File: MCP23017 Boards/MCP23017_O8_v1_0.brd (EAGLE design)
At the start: 90 x 90 mm, 83 parts, among them IC3 74HC540N, IC4 74HC540N, IC5 MCP23017SP, X4 057-016-0

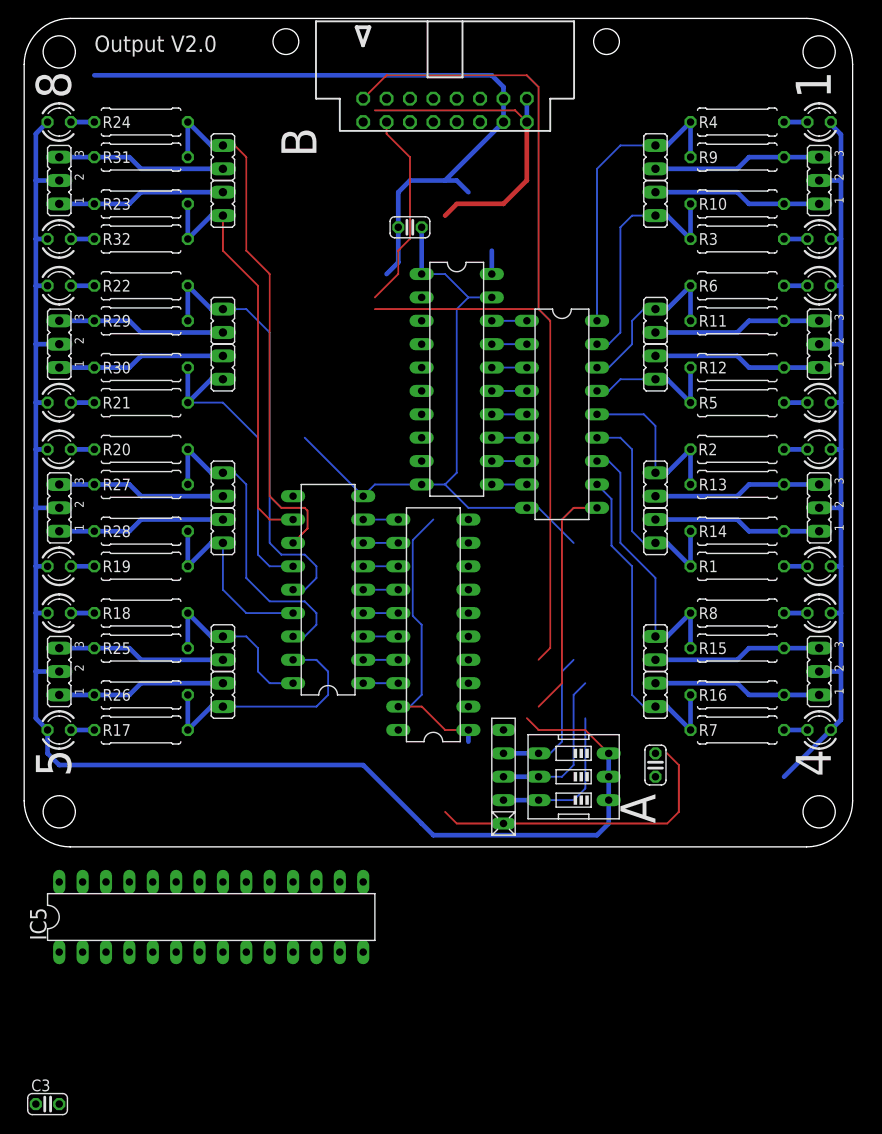
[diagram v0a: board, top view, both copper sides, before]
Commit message: Update MCP23017_O8_v1_0.brd
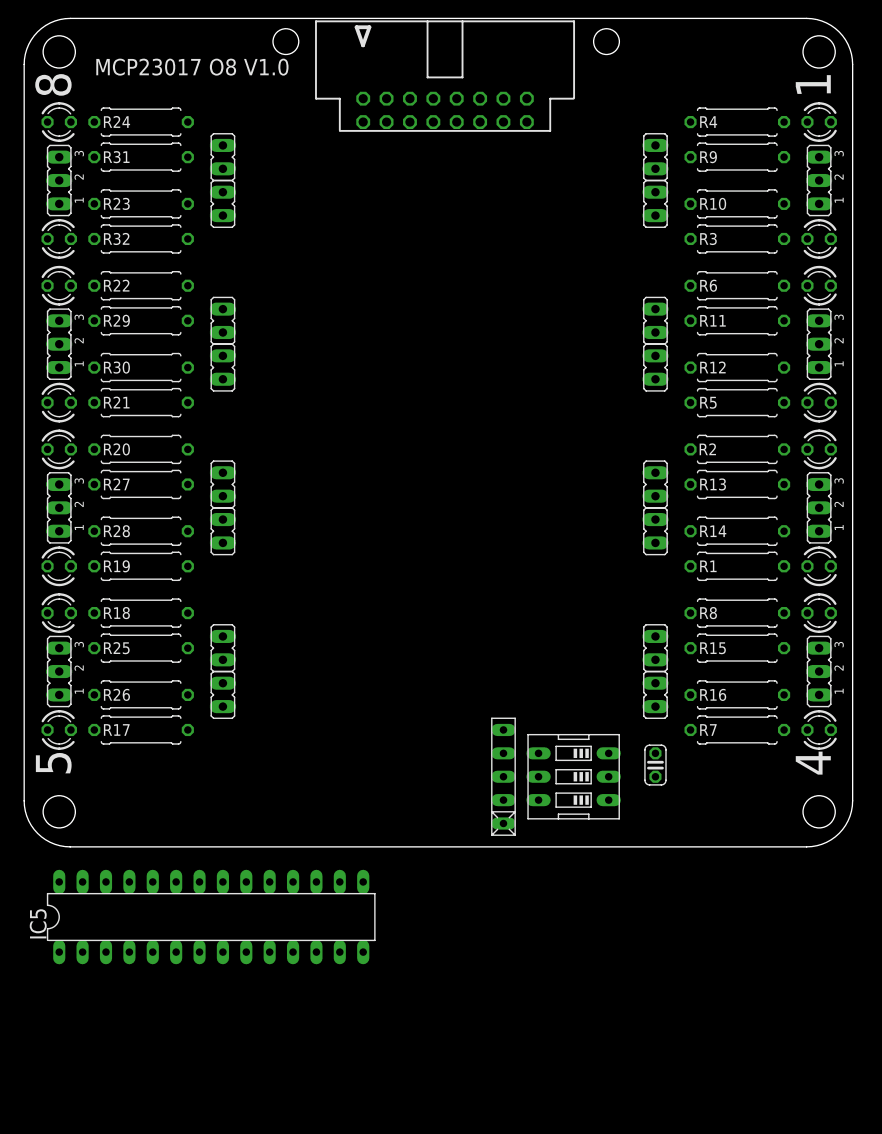
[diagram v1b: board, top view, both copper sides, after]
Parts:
- removed C3, C6: 100nF, resistor:C025-024X044
- removed IC1, IC2: (no value), uln-udn:DIL18
- removed IC3, IC4: 74HC540N, 74xx-eu:DIL20
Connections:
- removed net N$12: IC2.8, IC3.11
- removed net N$14: IC2.7, IC3.12
- removed net N$15: IC2.6, IC3.13
- removed net N$16: IC2.5, IC3.14
- removed net N$17: IC2.4, IC3.15
- removed net N$18: IC2.3, IC3.16
- removed net N$19: IC2.2, IC3.17
- removed net N$2: IC2.13, JP13.2, R1.2, R14.1
- removed net N$20: IC2.1, IC3.18
- removed net N$21: IC3.2, IC5.21
- removed net N$23: IC3.4, IC5.23
- removed net N$25: IC3.6, IC5.25
- removed net N$27: IC3.8, IC5.27
- removed net N$31: IC2.17, JP16.2, R10.1, R3.2
- removed net N$34: IC1.8, IC4.11
- removed net N$38: IC2.11, JP15.2, R16.1, R7.2
- removed net N$39: IC1.7, IC4.12
- removed net N$40: IC1.6, IC4.13
- removed net N$42: IC2.15, JP11.2, R12.1, R5.2
- removed net N$44: IC1.5, IC4.14
- removed net N$45: IC1.4, IC4.15
- removed net N$46: IC1.3, IC4.16
- removed net N$47: IC1.2, IC4.17
- removed net N$48: IC1.1, IC4.18
- removed net N$50: IC4.3, IC5.2
- removed net N$52: IC4.5, IC5.4
- removed net N$55: IC4.6, IC5.5
- removed net N$57: IC4.8, IC5.7
- removed net N$59: IC1.18, JP17.2, R18.2, R25.1
- removed net N$63: IC1.16, JP18.2, R20.2, R27.1
- removed net N$68: IC1.13, JP21.2, R21.2, R30.1
- removed net N$83: IC1.11, JP23.2, R23.2, R32.1
- net GND2: no longer C3.1, C6.1, IC1.9, IC2.9, IC3.1, IC3.10, IC3.19, IC4.1, IC4.10, IC4.19
- net N$22: now also JP16.2, R10.1, R3.2; no longer IC3.3
- net N$24: now also JP11.2, R12.1, R5.2; no longer IC3.5
- net N$26: now also JP13.2, R1.2, R14.1; no longer IC3.7
- net N$28: now also JP15.2, R16.1, R7.2; no longer IC3.9
- net N$29: now also IC5.21; no longer IC2.18
- net N$41: now also IC5.23; no longer IC2.16
- net N$43: now also IC5.25; no longer IC2.14
- net N$49: now also JP17.2, R18.2, R25.1; no longer IC4.2
- net N$5: now also IC5.27; no longer IC2.12
- net N$51: now also JP18.2, R20.2, R27.1; no longer IC4.4
- net N$56: now also JP21.2, R21.2, R30.1; no longer IC4.7
- net N$58: now also JP23.2, R23.2, R32.1; no longer IC4.9
- net N$60: now also IC5.2; no longer IC1.17
- net N$64: now also IC5.4; no longer IC1.15
- net N$65: now also IC5.5; no longer IC1.14
- net N$71: now also IC5.7; no longer IC1.12
- net VCC5.1: no longer C3.2, C6.2, IC1.10, IC2.10, IC3.20, IC4.20
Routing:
- net VCC5.1: track 365.0 -> 0.00 mm
- net GND2: track 173.2 -> 0.00 mm
- net N$82: track 101.7 -> 0.00 mm
- net N$71: track 58.5 -> 0.00 mm
- net N$65: track 48.1 -> 0.00 mm
- net N$83: track 46.3 -> 0.00 mm
- net N$38: track 36.2 -> 0.00 mm
- net N$63: track 35.4 -> 0.00 mm
- net N$68: track 34.9 -> 0.00 mm
- net N$29: track 32.6 -> 0.00 mm
- net N$5: track 31.1 -> 0.00 mm
- net N$60: track 27.5 -> 0.00 mm
- net N$31: track 27.5 -> 0.00 mm
- net N$2: track 25.0 -> 0.00 mm
- net N$64: track 22.4 -> 0.00 mm
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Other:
- board text added: "MCP23017 O8 V1.0"
- board text removed: "A"
- board text removed: "B"
- board text removed: "Output V2.0"

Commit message: Update MCP23017_O8_v1_0.brd
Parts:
- moved C2 63.2 mm to (44.5, 67.3), turned to 0 degrees
- moved IC5 58.5 mm to (44.5, 45.7), turned to 270 degrees
- moved RN2 15.3 mm to (50.8, 22.9), turned to 0 degrees
- moved SW1 10.2 mm to (50.8, 12.7), turned to 0 degrees

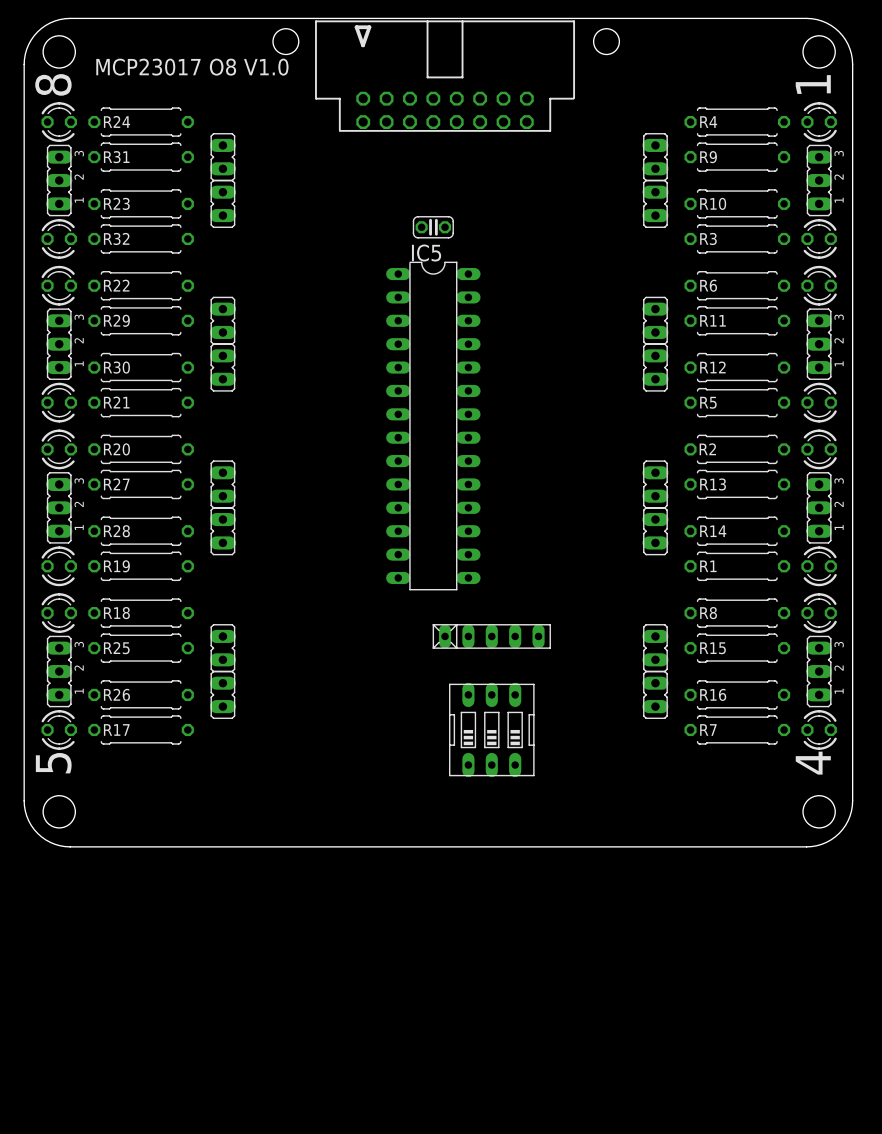
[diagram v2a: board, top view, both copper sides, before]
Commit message: Update MCP23017_O8_v1_0.brd
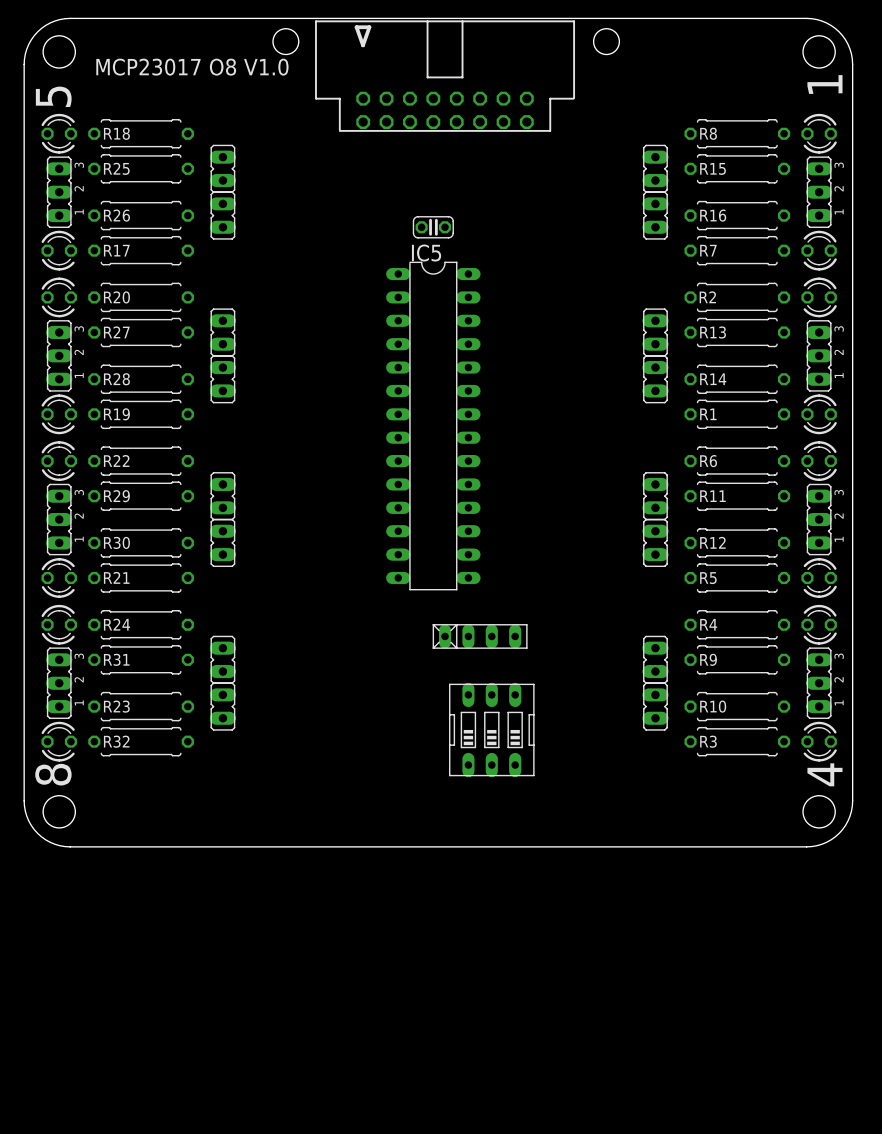
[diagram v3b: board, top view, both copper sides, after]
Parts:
- RN2: device resistor-net:RN-5 -> resistor-net_edit:RN-3
- moved JP22 54.6 mm to (21.6, 20.3)
- moved JP9 54.6 mm to (68.6, 20.3)
- moved R23 54.6 mm to (12.7, 11.4)
- moved R3 54.6 mm to (77.5, 11.4)
- moved R31 54.6 mm to (12.7, 20.3)
- moved R9 54.6 mm to (77.5, 20.3)
- moved SIG_15 54.6 mm to (3.81, 11.4)
- moved SIG_2 54.6 mm to (86.4, 11.4)
- moved JP1 54.6 mm to (86.4, 17.8)
- moved JP8 54.6 mm to (3.81, 17.8)
- moved R24 54.6 mm to (12.7, 24.1)
- moved R4 54.6 mm to (77.5, 24.1)
- moved SIG_1 54.6 mm to (86.4, 24.1)
- moved SIG_16 54.6 mm to (3.81, 24.1)
- moved JP16 54.6 mm to (68.6, 15.2)
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
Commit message: Update MCP23017_O8_v1_0.brd
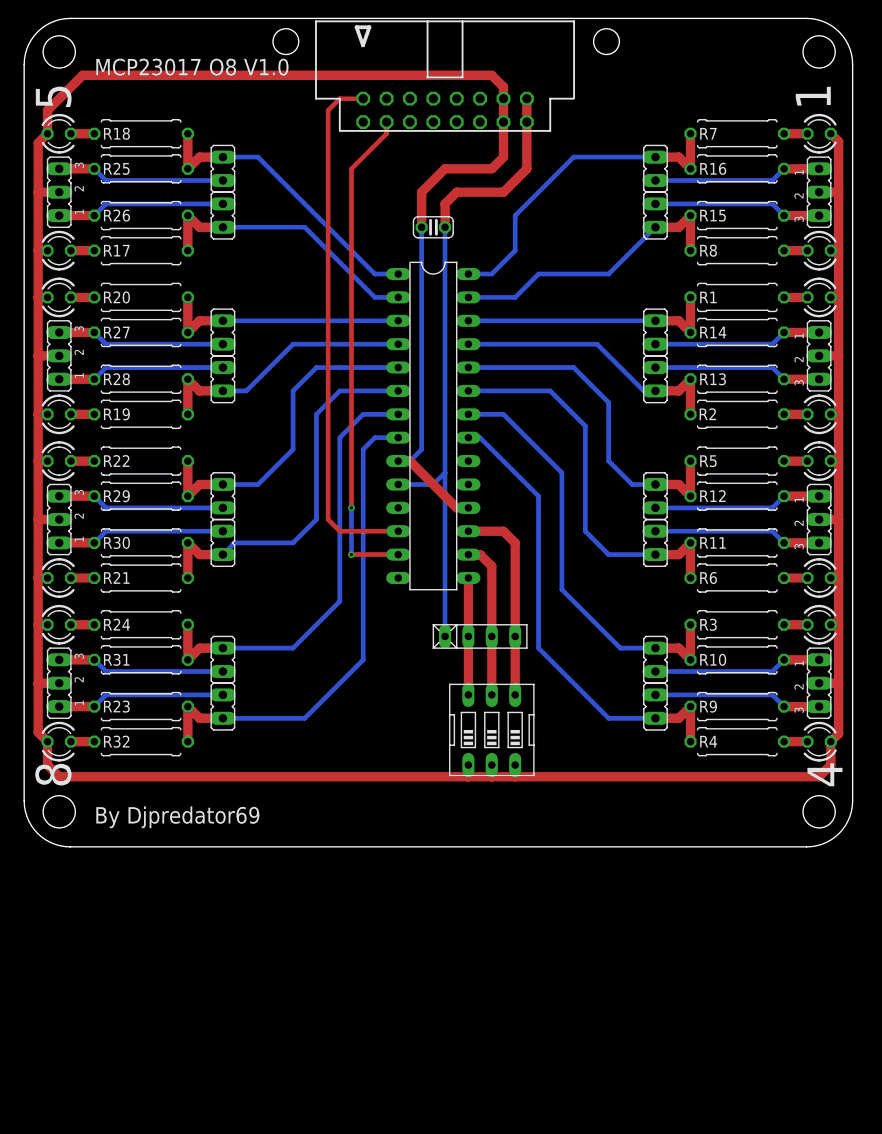
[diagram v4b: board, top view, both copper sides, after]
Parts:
- moved R7 12.7 mm to (77.5, 77.5)
- moved R8 12.7 mm to (77.5, 64.8)
- moved SIG_7 12.7 mm to (86.4, 64.8)
- moved SIG_8 12.7 mm to (86.4, 77.5)
- moved R3 12.7 mm to (77.5, 24.1)
- moved R4 12.7 mm to (77.5, 11.4)
- moved SIG_1 12.7 mm to (86.4, 11.4)
- moved SIG_2 12.7 mm to (86.4, 24.1)
- moved R1 12.7 mm to (77.5, 59.7)
- moved R2 12.7 mm to (77.5, 47.0)
- moved R5 12.7 mm to (77.5, 41.9)
- moved R6 12.7 mm to (77.5, 29.2)
- moved SIG_3 12.7 mm to (86.4, 29.2)
- moved SIG_4 12.7 mm to (86.4, 41.9)
- moved SIG_5 12.7 mm to (86.4, 47.0)
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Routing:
- net VCC5.1: track 0.00 -> 370.4 mm
- net GND2: track 0.00 -> 70.7 mm
- net N$82: track 0.00 -> 56.9 mm
- net N$84: track 0.00 -> 53.6 mm, vias 0 -> 2
- net N$58: track 0.00 -> 53.2 mm
- net N$29: track 0.00 -> 50.8 mm
- net N$71: track 0.00 -> 48.1 mm
- net N$22: track 0.00 -> 46.4 mm
- net N$41: track 0.00 -> 42.5 mm
- net N$56: track 0.00 -> 41.3 mm
- net N$24: track 0.00 -> 37.4 mm
- net N$65: track 0.00 -> 36.2 mm
- net N$28: track 0.00 -> 36.0 mm
- net N$49: track 0.00 -> 32.5 mm
- net N$5: track 0.00 -> 31.6 mm
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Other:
- board text added: "By Djpredator69"
